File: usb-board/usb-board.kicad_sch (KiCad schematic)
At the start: 14 parts, among them J1 Conn_01x06, J2 USB_C_Receptacle_USB2.0

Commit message: usb-board: add silkscreen markings
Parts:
- H5, H6: now left out of the parts list
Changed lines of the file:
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@@
   )
   (symbol (lib_id "Mechanical:MountingHole") (at 267.97 40.64 0) (unit 1)
-    (in_bom yes) (on_board yes) (dnp no) (fields_autoplaced)
+    (in_bom no) (on_board yes) (dnp no) (fields_autoplaced)
     (property "Reference" "H5" (at 270.51 39.4279 0)
       (effects (font (size 1.27 1.27)) (justify left))
@@
   )
   (symbol (lib_id "Mechanical:MountingHole") (at 267.97 45.72 0) (unit 1)
-    (in_bom yes) (on_board yes) (dnp no) (fields_autoplaced)
+    (in_bom no) (on_board yes) (dnp no) (fields_autoplaced)
     (property "Reference" "H6" (at 270.51 44.5079 0)
       (effects (font (size 1.27 1.27)) (justify left))

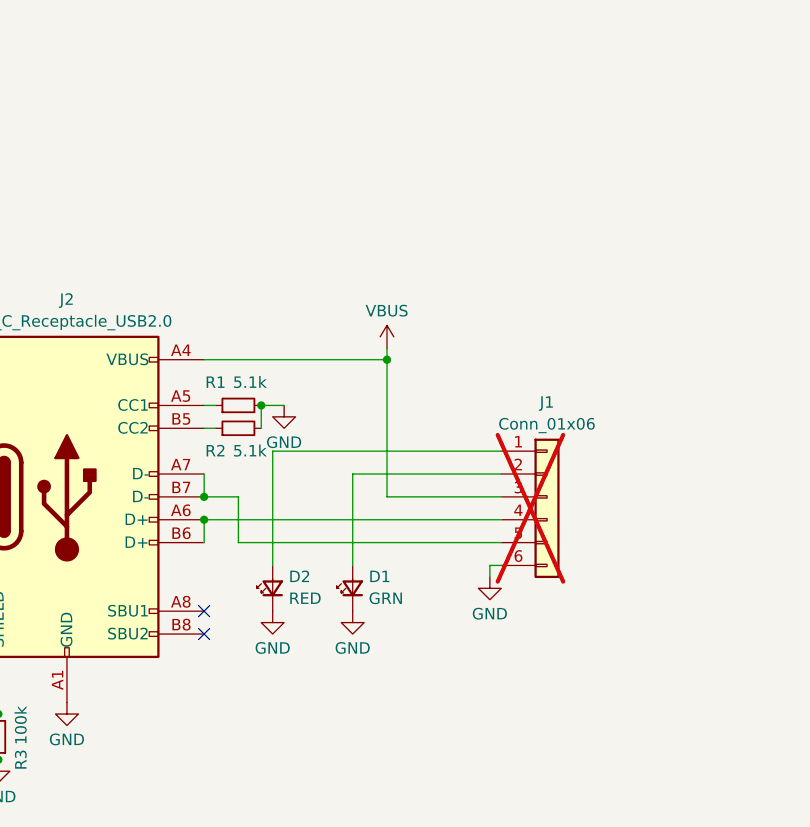
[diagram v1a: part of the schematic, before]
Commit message: Change mainboard connector to FFC type
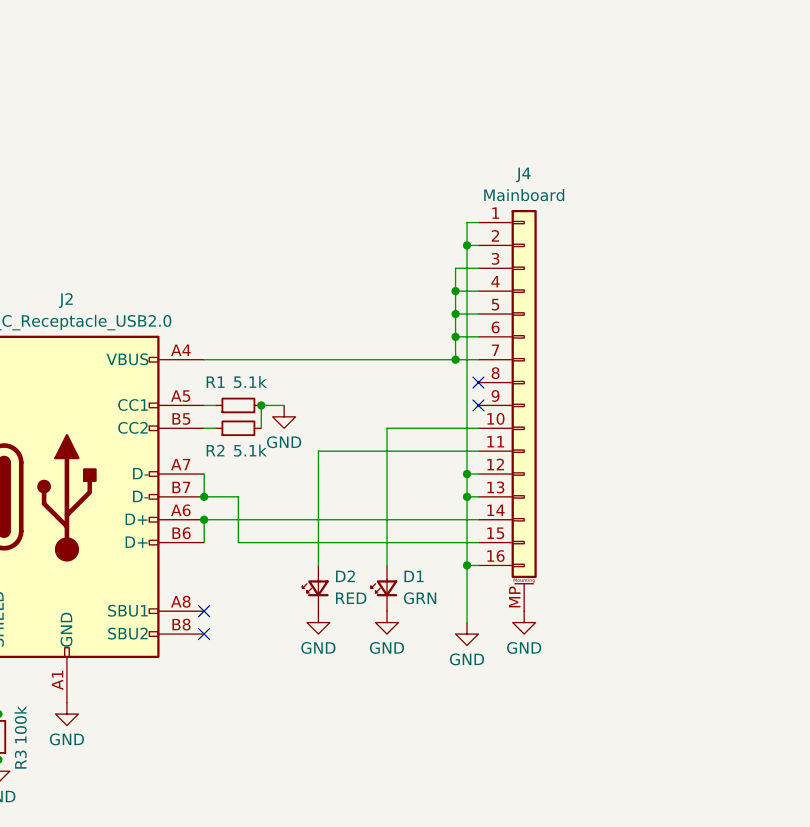
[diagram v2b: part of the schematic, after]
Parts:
- removed J1: Conn_01x06, Connector_PinHeader_2.00mm:PinHeader_1x06_P2.00mm_Vertical, symbol Connector_Generic:Conn_01x06
- added J4: Mainboard, Connector_FFC-FPC_HDGC:0.5K-QX-16PWB_16Pin_0.5mm, symbol Connector_Generic_MountingPin:Conn_01x16_MountingPin
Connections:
- net GND: now also J4.1 (Pin_1), J4.12 (Pin_12), J4.13 (Pin_13), J4.16 (Pin_16), J4.2 (Pin_2), J4.MP (MountPin)
- net at D2.2 (A): now also J4.11 (Pin_11)
- net at D1.2 (A): now also J4.10 (Pin_10)
- net at J2.A6 (D+), J2.B6 (D+): now also J4.14 (Pin_14)
- net at J2.A7 (D-), J2.B7 (D-): now also J4.15 (Pin_15)
- net VBUS: no longer names the net of J2.A4 (VBUS), J2.A9 (VBUS), J2.B4 (VBUS), J2.B9 (VBUS)
- net VBUS: now also J4.3 (Pin_3), J4.4 (Pin_4), J4.5 (Pin_5), J4.6 (Pin_6), J4.7 (Pin_7)
- no-connect marks 2 -> 4
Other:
- moved on the sheet: D1, D2

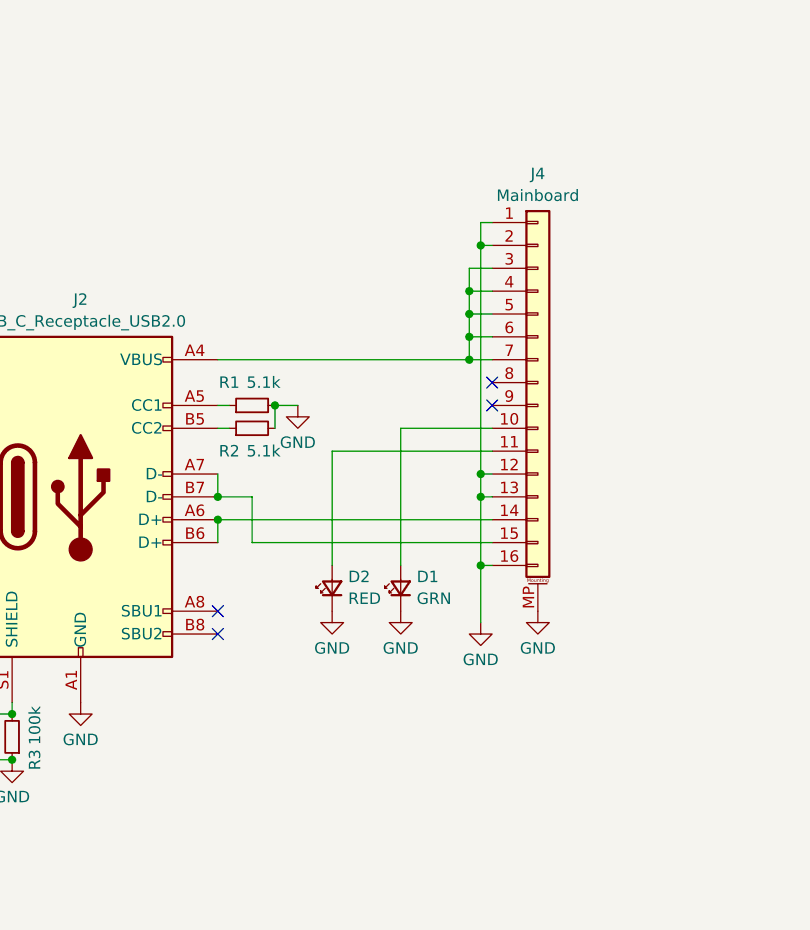
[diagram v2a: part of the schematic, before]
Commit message: usb-board: fix FFC pinout
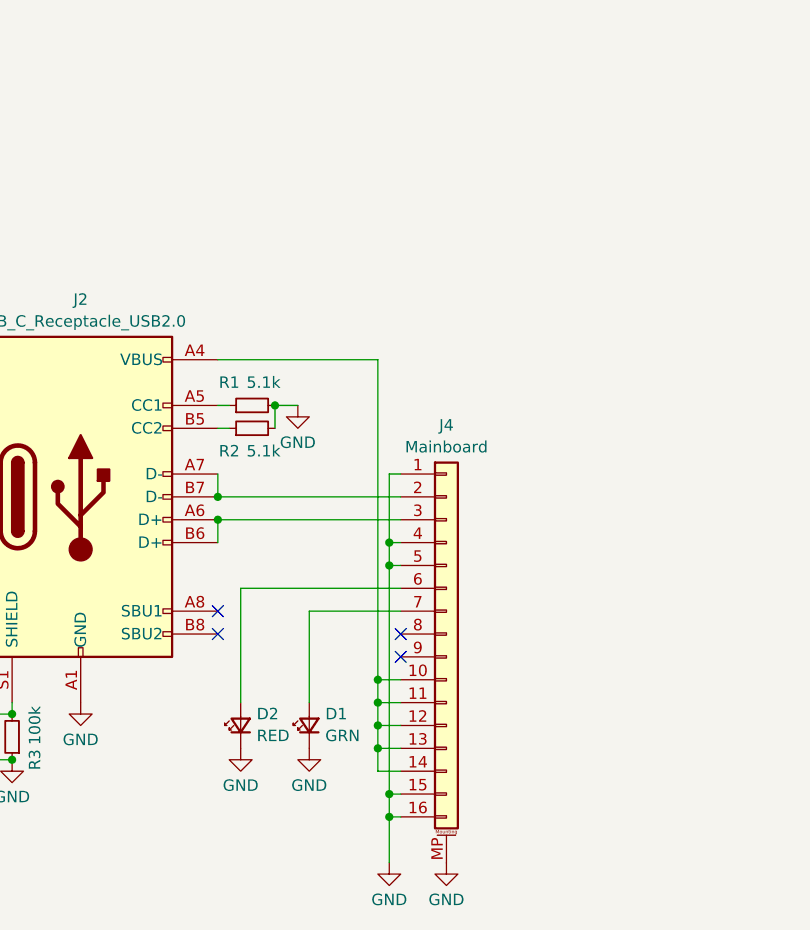
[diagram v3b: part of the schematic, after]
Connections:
- net GND: now also J4.15 (Pin_15), J4.4 (Pin_4), J4.5 (Pin_5); no longer J4.12 (Pin_12), J4.13 (Pin_13), J4.2 (Pin_2)
- net at J4.10 (Pin_10): now also J2.A4 (VBUS), J2.A9 (VBUS), J2.B4 (VBUS), J2.B9 (VBUS), J4.11 (Pin_11), J4.12 (Pin_12), J4.13 (Pin_13), J4.14 (Pin_14); no longer D1.2 (A)
- net at D2.2 (A): now also J4.6 (Pin_6); no longer J4.11 (Pin_11)
- net at J2.A6 (D+), J2.B6 (D+): now also J4.3 (Pin_3); no longer J4.14 (Pin_14)
- net at J2.A7 (D-), J2.B7 (D-): now also J4.2 (Pin_2); no longer J4.15 (Pin_15)
- new net: D1.2 (A), J4.7 (Pin_7)
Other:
- moved on the sheet: D1, D2, J4
